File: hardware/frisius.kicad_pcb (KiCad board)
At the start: 4 copper layers, 40 x 60 mm, 133 parts, among them J1 Conn_02x20_Odd_Even_Shielded, J3 USB_C_Receptacle, J4 MEM2067, Q1 Q_NMOS_DGS, Q2 MBT2222ADW1T1, SW1 OVERRIDE, SW4 SW_Push, U1 ESP32-PICO-V3-02, U10 CP2102N-Axx-xQFN24, U12 RT5789, U2 FXOS8700CQR1, U3 MS5637-02BA03, U4 L96-M33, U5 MAX77751, U6 LM75B, U7 MAX17048G, U8 NCV8187AMLExCG, U9 NCV8187AMLExCG

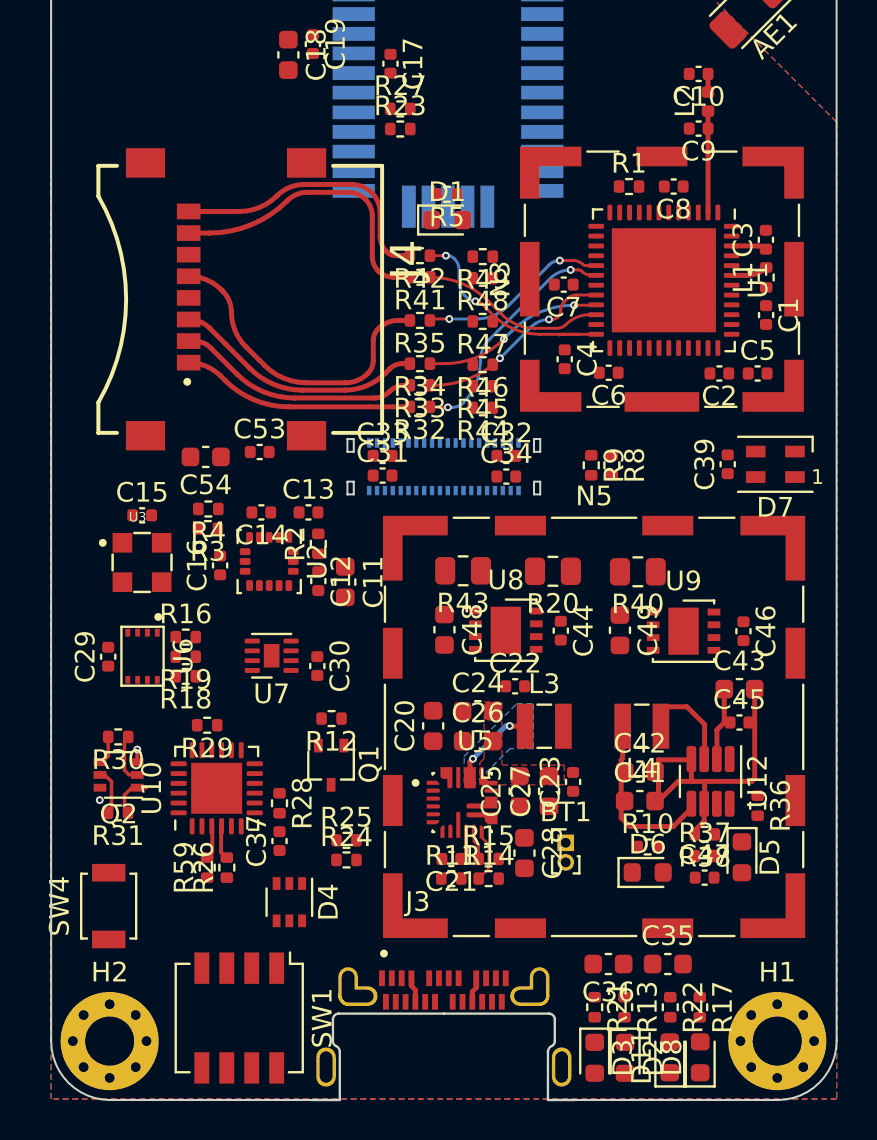
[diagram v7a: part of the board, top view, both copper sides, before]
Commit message: screen mock, tweaked layout easier powerplane division
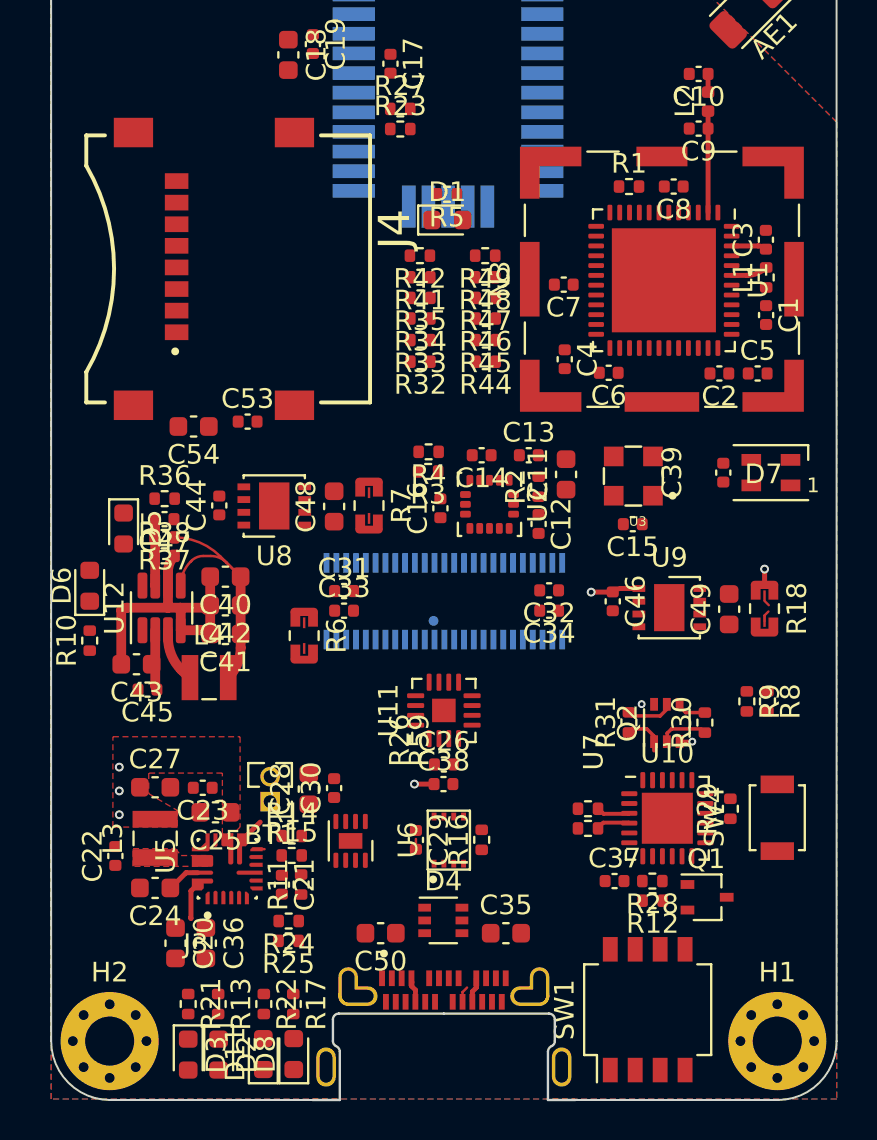
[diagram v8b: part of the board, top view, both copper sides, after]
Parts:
- removed N5: SheildCan_Power, RF_Shielding:Wuerth_36103205_20x20mm
- removed R19: 4.7k, Resistor_SMD:R_0402_1005Metric
- removed R20, R40, R43: 0, Resistor_SMD:R_0805_2012Metric
- added C38: 0.1u, Capacitor_SMD:C_0402_1005Metric, F.Cu at (144.0, 114.0)
- added C40: 10u, Capacitor_SMD:C_0603_1608Metric, F.Cu at (132.9, 103.4)
- added C50: 4.7u, Capacitor_SMD:C_0603_1608Metric, F.Cu at (140.8, 121.6)
- added N6: Display Board, Fiducial:Fiducial_0.5mm_Mask1.5mm, B.Cu at (143.5, 102.7)
- added R6: DISP_SENSE, bt_Resistor:R_0805_4WKelvin, F.Cu at (136.9, 106.4)
- added R7: AUX_SENSE, bt_Resistor:R_0805_4WKelvin, F.Cu at (140.2, 99.8)
- added U11: PAC194x-1, bt_Package_QFN:VQFN-16-1EP_3x3mm_P0.5mm_EP1.2x1.2mm, F.Cu at (144.0, 110.2)
- BT1: footprint Connector_PinHeader_1.00mm:PinHeader_1x02_P1.00mm_Vertical -> Connector_PinHeader_1.27mm:PinHeader_1x02_P1.27mm_Vertical
- C26: value 10u -> 1u; footprint Capacitor_SMD:C_0603_1608Metric -> Capacitor_SMD:C_0402_1005Metric
- J1: value Conn_02x20_Odd_Even_Shielded -> Conn_02x25_Odd_Even_Shielded; footprint Connector_Molex:Molex_SlimStack_502426-4010_2x20_P0.40mm_Vertical -> Connector_Molex:Molex_SlimStack_55560-0501_2x25_P0.50mm_Vertical
- R18: value 4.7k -> CORE_SENSE; footprint Resistor_SMD:R_0402_1005Metric -> bt_Resistor:R_0805_4WKelvin
- SW1: footprint Button_Switch_SMD:SW_DIP_SPSTx04_Slide_Copal_CHS-04A_W5.08mm_P1.27mm_JPin -> Button_Switch_SMD:SW_DIP_SPSTx04_Slide_Omron_A6H-4101_W6.15mm_P1.27mm
- moved D5 35.7 mm to (127.7, 101.0)
- moved SW4 34.3 mm to (161.0, 115.7)
- moved R36 34.0 mm to (129.8, 99.5), turned to 0 degrees
- moved C47 33.0 mm to (129.8, 100.5), turned to 180 degrees
- moved D6 31.9 mm to (126.0, 103.9), turned to 90 degrees
- moved R37 31.9 mm to (129.8, 101.4), turned to 180 degrees
- moved R38 31.0 mm to (129.8, 102.4), turned to 0 degrees
- moved C43 30.7 mm to (128.4, 107.9), turned to 180 degrees
- moved R10 30.3 mm to (126.0, 106.7), turned to 90 degrees
- moved C45 30.2 mm to (128.9, 109.2), turned to 180 degrees
- moved R30 29.9 mm to (157.3, 110.9), turned to 90 degrees
- moved R18 29.7 mm to (160.3, 105.0), turned to -90 degrees
- moved U12 29.3 mm to (129.6, 105.0), turned to 90 degrees
- moved Q2 28.0 mm to (155.4, 110.9), turned to 90 degrees
- moved R29 27.0 mm to (158.6, 115.2), turned to 90 degrees
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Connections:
- C26 pad 1: VBUS_OVP -> VDD_NVDC
- C29 pad 1: VDD_NVDC -> +BATT
- C29 pad 2: Net-(C29-Pad2) -> GND
- C31 pad 1: VDD_DISP_3V3 -> VDD_DISP_3V5
- C33 pad 1: VDD_DISP_3V3 -> VDD_DISP_3V5
- D2 pad 2: VDD_CORE_3V3 -> VDD_NVDC
- D3 pad 2: VDD_CORE_3V3 -> VDD_NVDC
- D4 pad 5: GND -> unconnected-(D4-Pad5)
- J1 pad 1: GND -> unconnected-(J1-Pad1)
- J1 pad 10: VDD_DISP_3V3 -> GND
- J1 pad 11: GND -> VDD_DISP_3V5
- J1 pad 12: GND -> VDD_DISP_3V5
- J1 pad 13: unconnected-(J1-Pad13) -> VDD_DISP_3V5
- J1 pad 14: unconnected-(J1-Pad14) -> VDD_DISP_3V5
- J1 pad 15: /Display B2B/STATUS_LED_EXT -> VDD_DISP_3V5
- J1 pad 16: /Display B2B/SPARE_0 -> VDD_DISP_3V5
- J1 pad 18: /Display B2B/SPARE_1 -> GND
- J1 pad 19: /Display B2B/DISPLAY.MOSI -> unconnected-(J1-Pad19)
- J1 pad 2: GND -> unconnected-(J1-Pad2)
- J1 pad 20: /Display B2B/SPARE_2 -> unconnected-(J1-Pad20)
- J1 pad 21: /Display B2B/DISPLAY.MISO -> /Display B2B/STATUS_LED_EXT
- J1 pad 22: GND -> /Display B2B/SPARE_0
- J1 pad 23: /Display B2B/DISPLAY.SCLK -> GND
- J1 pad 24: /Display B2B/USR_BTN.NAV_A -> /Display B2B/SPARE_1
- J1 pad 25: /Display B2B/DISPLAY.CS -> /Display B2B/DISPLAY.MOSI
- J1 pad 26: /Display B2B/USR_BTN.PWR -> /Display B2B/SPARE_2
- J1 pad 27: /Display B2B/DISPLAY.DC -> /Display B2B/DISPLAY.MISO
- J1 pad 29: GND -> /Display B2B/DISPLAY.SCLK
- J1 pad 3: GND -> unconnected-(J1-Pad3)
- J1 pad 30: /BMS/SENSOR_I2C.SDA -> /Display B2B/USR_BTN.NAV_A
- J1 pad 31: /Display B2B/DISPLAY.BL -> /Display B2B/DISPLAY.CS
- J1 pad 32: /BMS/SENSOR_I2C.SCL -> /Display B2B/USR_BTN.PWR
- J1 pad 33: GND -> /Display B2B/DISPLAY.DC
- J1 pad 35: VDD_NVDC -> GND
- J1 pad 36: VDD_NVDC -> /BMS/SENSOR_I2C.SDA
- J1 pad 37: VDD_NVDC -> /Display B2B/DISPLAY.BL
- J1 pad 38: VDD_NVDC -> /BMS/SENSOR_I2C.SCL
- J1 pad 4: GND -> unconnected-(J1-Pad4)
- J1 pad 5: VDD_DISP_3V3 -> unconnected-(J1-Pad5)
- J1 pad 6: VDD_DISP_3V3 -> unconnected-(J1-Pad6)
- J1 pad 7: VDD_DISP_3V3 -> GND
- J1 pad 8: VDD_DISP_3V3 -> GND
- J1 pad 9: VDD_DISP_3V3 -> GND
- R11 pad 2: VDD_CORE_3V3 -> VDD_NVDC
- R18 pad 1: VDD_AUX_3V3 -> VDD_CORE_3V3
- R18 pad 2: /BMS/SENSOR_I2C.SDA -> /Power/VDD_CORE_SNS-
- U6 pad 4: Net-(C29-Pad2) -> GND
- U6 pad 8: VDD_NVDC -> +BATT
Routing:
- net Net-(J4-Pad5): track 16.1 -> 0.00 mm
- net Net-(J4-Pad7): track 15.1 -> 0.00 mm
- net Net-(J4-Pad8): track 14.1 -> 0.00 mm
- net Net-(J4-Pad3): track 12.8 -> 0.00 mm
- net Net-(J4-Pad2): track 12.3 -> 0.00 mm
- net /Processor/SDMMC.D2: track 12.2 -> 0.00 mm, vias 2 -> 0
- net Net-(J4-Pad1): track 11.8 -> 0.00 mm
- net /Processor/SDMMC.D1: track 11.6 -> 0.00 mm, vias 2 -> 0
- net /Processor/SDMMC.D3: track 10.2 -> 0.00 mm, vias 2 -> 0
- net /Processor/SDMMC.CLK: track 9.64 -> 0.01 mm, vias 2 -> 0
- net /Processor/SDMMC.D0: track 9.38 -> 0.00 mm
- net /Processor/SDMMC.CMD: track 9.28 -> 0.25 mm, vias 2 -> 0
- net VDD_SYS_3V5: track 10.1 -> 16.2 mm, vias 0 -> 1
- net Net-(C22-Pad2): track 4.14 -> 0.00 mm, vias 2 -> 0
- net Net-(C47-Pad2): track 0.00 -> 3.38 mm
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- added copper zone on In1.Cu, net GND
- added copper zone on F.Cu, net Net-(C22-Pad2)
- added copper zone on In2.Cu, net VDD_AUX_3V3
- added copper zone on In2.Cu, net VDD_CORE_3V3
- added copper zone on F.Cu, net VDD_NVDC
- removed copper zone on B.Cu, net Net-(C22-Pad2)
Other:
- board text added: "AUX"
- board text added: "BATT"
- board text added: "CORE"
- board text added: "NVDC"
- board text added: "SYS"
- board text added: "VBUS"
